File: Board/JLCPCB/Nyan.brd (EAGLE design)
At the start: 86 x 26 mm, 64 parts, among them IC1 74HCT541PW, IC2 STM32F10XCXT6, IC3 74HCT541PW, IC4 ST3485, U2 A4988_STEP, U3 MAX6966, X1 WR-WTB2.0-2_THT-VER, X10 32768, X2 WR-WTB2.0-4_THT_VER, X3 WR-WTB2.0-5_THT-VER, X4 WR-WTB2.0-5_THT-VER, X6 68610614122, X7 68612414422, X8 68610414122, X9 8M

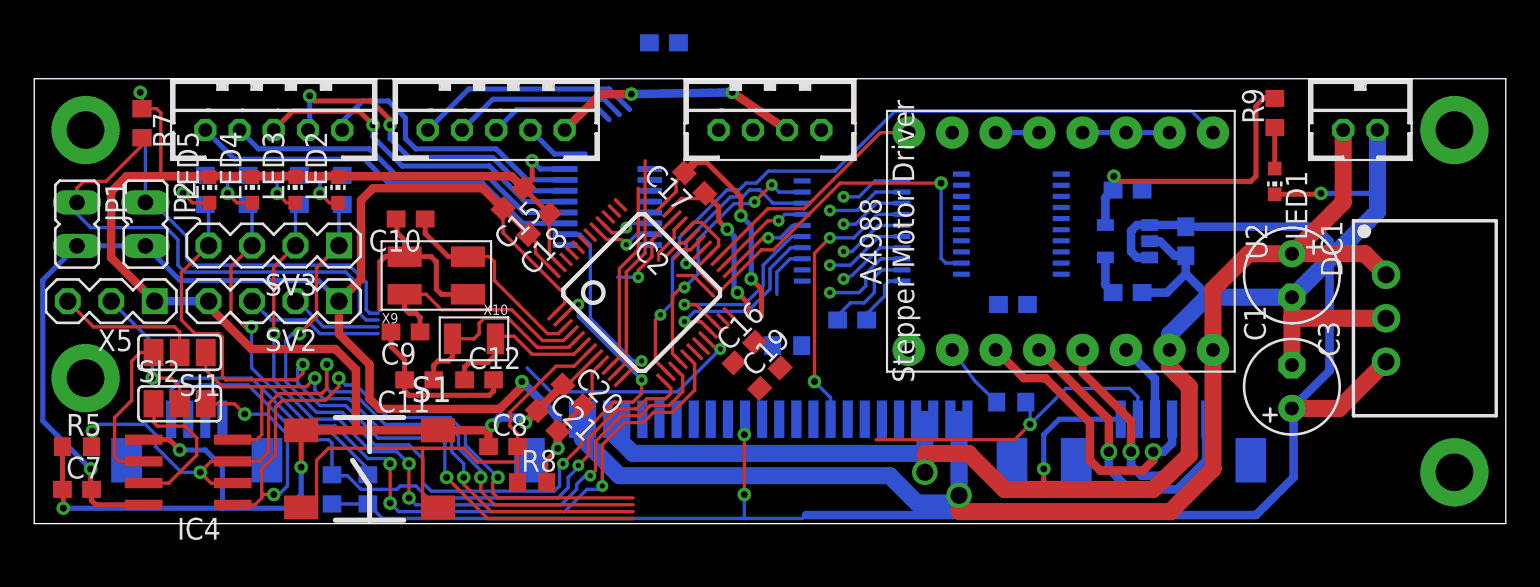
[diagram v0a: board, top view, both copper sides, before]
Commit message: [Board] Layouting of first half (microcontroller side) done.
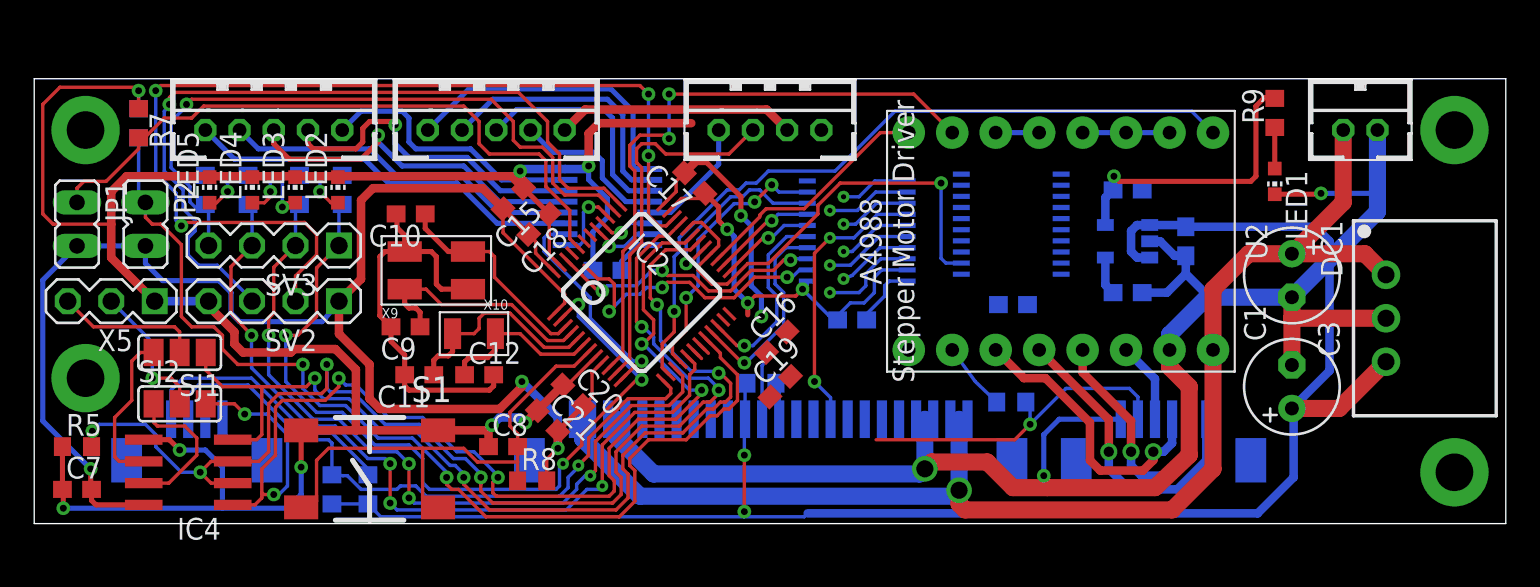
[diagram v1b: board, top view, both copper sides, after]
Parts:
- moved C4 13.7 mm to (33.5, 14.8), turned to 0 degrees
- moved R4 2.66 mm to (42.5, 8.20)
- moved C16 1.99 mm to (43.4, 10.6)
- moved C19 0.78 mm to (43.6, 8.00)
- moved IC1 0.30 mm to (48.1, 17.1)
- moved C10 0.30 mm to (22.0, 18.1)
- moved C9 0.30 mm to (21.7, 11.5)
- moved X9 0.30 mm to (23.5, 14.8)
- moved C11 0.30 mm to (22.5, 8.70)
- moved C12 0.30 mm to (26.0, 8.70)
- moved X10 0.30 mm to (25.7, 11.1)
- moved R6 0.20 mm to (6.10, 23.4)
- moved R7 0.20 mm to (6.10, 23.4)
- moved R8 0.10 mm to (29.1, 2.50)
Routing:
- net SWDIO: track 11.1 -> 59.4 mm, vias 1 -> 4
- net SWCLK: track 8.16 -> 45.9 mm, vias 0 -> 1
- net GND: track 261.5 -> 298.3 mm, vias 12 -> 14
- net MOT_STP: track 11.2 -> 36.5 mm, vias 0 -> 2
- net BOOT1: track 35.9 -> 60.4 mm, vias 1 -> 2
- net TX: track 38.0 -> 59.5 mm, vias 2 -> 4
- net RTS: track 49.9 -> 69.8 mm, vias 4 -> 6
- net RX: track 46.1 -> 65.7 mm, vias 4 -> 6
- net D1: track 0.00 -> 17.3 mm, vias 0 -> 3
- net D2: track 5.70 -> 16.6 mm, vias 0 -> 3
- net BOOT0: track 28.8 -> 38.5 mm
- net BUT_SIG: track 13.2 -> 21.7 mm
- net BUT_LED: track 0.00 -> 7.19 mm
- net LED8: track 7.35 -> 13.4 mm
- net FREE_LED: track 3.78 -> 9.29 mm
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
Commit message: [Board] More layouting
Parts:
- moved R4 5.83 mm to (44.7, 2.80), flipped to the top
- moved C19 2.06 mm to (43.1, 10.0), flipped to the bottom, turned to 90 degrees
- moved C16 0.67 mm to (43.1, 10.0), turned to 90 degrees
- moved R3 0.60 mm to (57.7, 7.10)
- moved C13 0.50 mm to (63.9, 14.0)
- moved C14 0.50 mm to (63.9, 19.0)
- moved C2 0.40 mm to (66.9, 16.5)
- moved R8 0.10 mm to (29.0, 2.50)
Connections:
- net +3V3: now also R1.2, R2.2, R4.2
- net +5V: no longer R1.2, R2.2, R4.2
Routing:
- net +5V: track 119.1 -> 61.1 mm
- net LATCH_5V: track 0.00 -> 30.7 mm, vias 0 -> 2
- net +3V3: track 134.7 -> 155.7 mm, vias 6 -> 9
- net GND: track 298.3 -> 315.2 mm, vias 14 -> 18
- net MOT_THERM: track 20.2 -> 35.8 mm
- net HEAD_THERM: track 2.96 -> 13.2 mm, vias 0 -> 2
- net D5_5V: track 16.4 -> 7.05 mm
- net N$8: track 31.3 -> 27.9 mm
- net DCLK_5V: track 4.96 -> 7.28 mm, vias 1 -> 2
- net D6_5V: track 4.23 -> 6.54 mm, vias 1 -> 2
- net N$19: track 2.24 -> 0.00 mm
- net D1_5V: track 5.75 -> 7.77 mm, vias 1 -> 2
- net D4_5V: track 4.35 -> 6.31 mm, vias 1 -> 2
- net D3_5V: track 5.21 -> 7.18 mm, vias 1 -> 2
- net D2_5V: track 4.43 -> 6.39 mm, vias 1 -> 2
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
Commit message: [Board] almost complete, last gnd and 3v traces missing
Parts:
- moved IC3 0.40 mm to (57.1, 17.1)
- moved C5 0.10 mm to (57.2, 12.7)
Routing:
- net GND: track 315.2 -> 364.9 mm, vias 18 -> 23
- net +5V: track 61.1 -> 109.1 mm, vias 2 -> 5
- net +3V3: track 155.7 -> 187.9 mm, vias 9 -> 10
- net D6_5V: track 6.54 -> 26.5 mm, vias 2 -> 3
- net DCLK_5V: track 7.28 -> 25.7 mm
- net STROBE_5V: track 6.42 -> 23.3 mm
- net D5_5V: track 7.05 -> 18.9 mm
- net D2_5V: track 6.39 -> 17.7 mm
- net D4_5V: track 6.31 -> 17.3 mm
- net D1_5V: track 7.77 -> 16.8 mm
- net D3_5V: track 7.18 -> 16.0 mm
- net MOT_DIR: track 14.3 -> 19.0 mm, vias 0 -> 1
- net N$19: track 0.00 -> 1.74 mm
- net BUT_SIG: track 21.7 -> 23.0 mm, vias 0 -> 1
- net HEAD_THERM: track 13.2 -> 14.3 mm

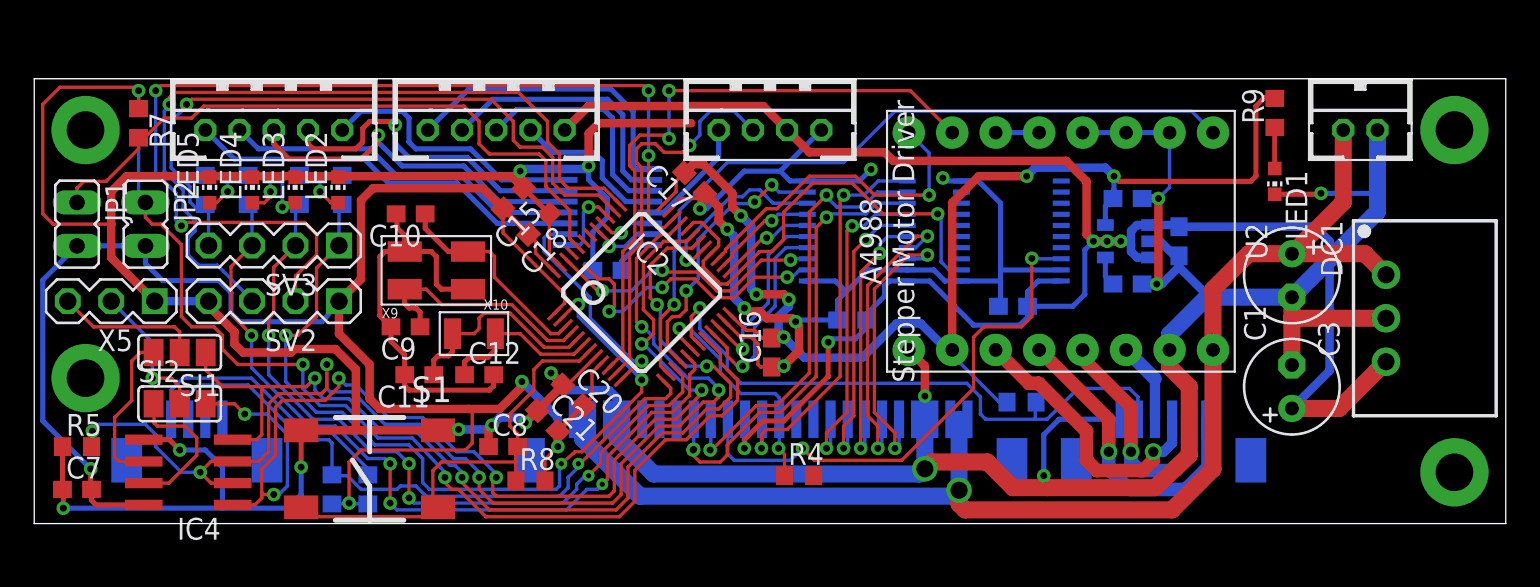
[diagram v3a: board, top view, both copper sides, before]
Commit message: [Board] Layout done
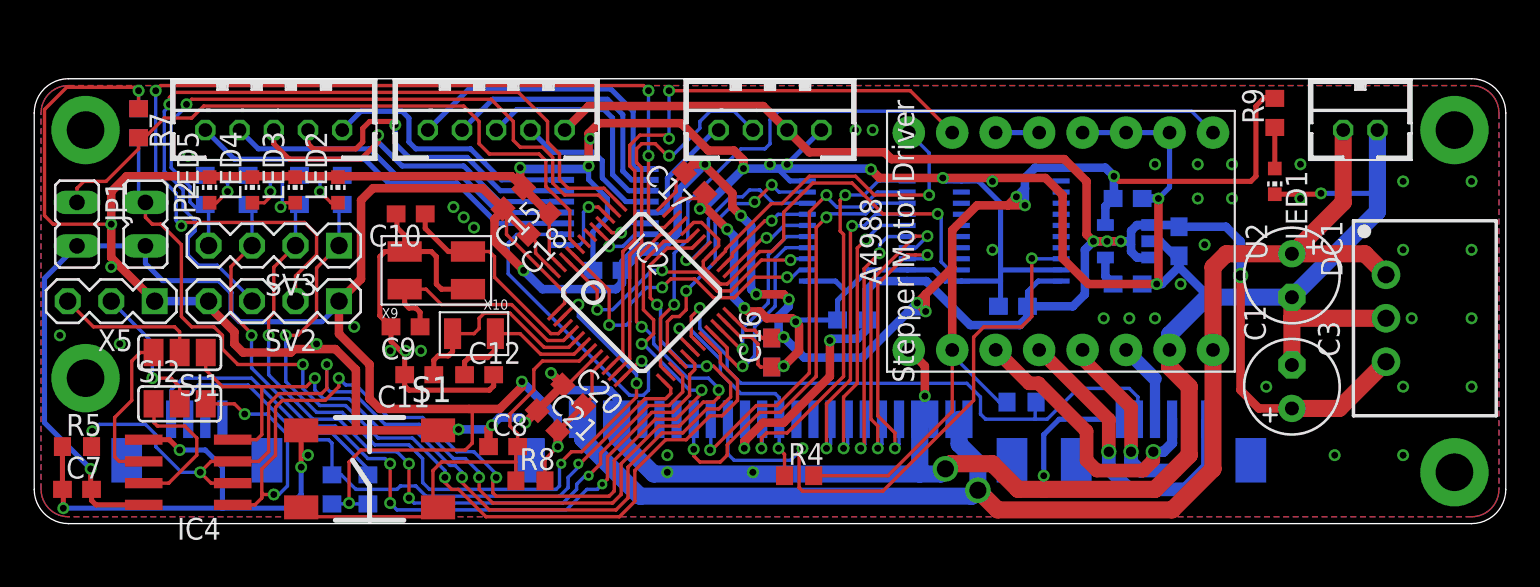
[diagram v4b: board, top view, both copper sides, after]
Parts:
- moved U3 0.20 mm to (33.3, 18.5)
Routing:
- net +3V3: track 187.9 -> 226.2 mm, vias 10 -> 15
- net GND: track 364.9 -> 392.3 mm, vias 23 -> 71
- net LED_CS: track 12.9 -> 20.2 mm
- net LATCH_5V: track 30.9 -> 34.4 mm
- net +5V: track 109.1 -> 106.1 mm, vias 5 -> 6
- net D1: track 17.4 -> 19.5 mm
- net D2: track 16.6 -> 18.2 mm
- net MOT_EN: track 44.3 -> 45.2 mm
- net +12V: track 78.1 -> 78.8 mm
- net D6_5V: vias 3 -> 2
- added copper zone on layer 1, net GND
- added copper zone on layer 16, net GND
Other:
- outline, holes or cut-outs redrawn

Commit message: [Board] Silk Screen Top done
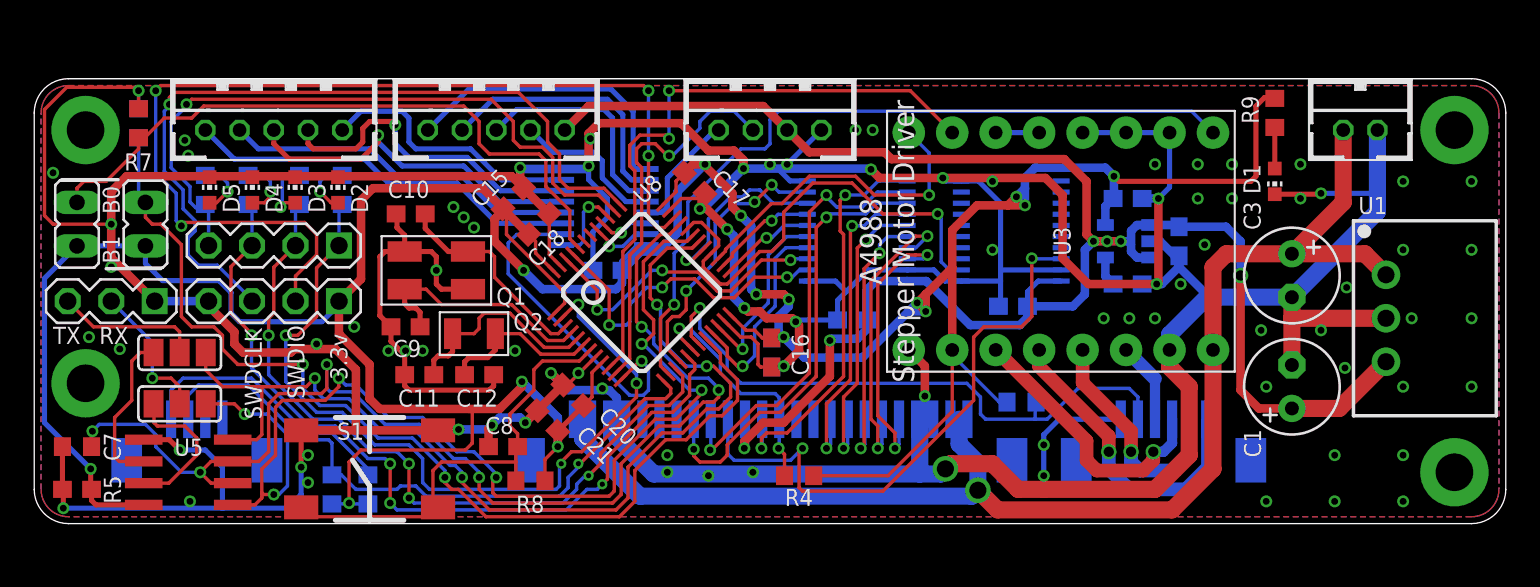
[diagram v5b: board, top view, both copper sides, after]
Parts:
- removed DC1: R-78C5.0-1.0, dc-dc-converter:SIP3
- added U4: MAX6966, meineLibrary:QSOP-16
- U1: value (none) -> R-78C5.0-1.0; device Power:SOT23-5 -> dc-dc-converter:SIP3
- U2: value A4988_STEP -> (none); device robotics:A4988_STEP -> Power:SOT23-5
- U3: value MAX6966 -> A4988_STEP; device meineLibrary:QSOP-16 -> robotics:A4988_STEP
- moved U3 26.8 mm to (60.0, 16.5), flipped to the top, turned to 270 degrees
- moved U1 15.8 mm to (79.0, 12.0), flipped to the top
- moved U2 3.90 mm to (63.9, 16.5), flipped to the bottom
- renumbered IC1 to U6, IC2 to U8, IC3 to U7, IC4 to U5, LED1 to D1, LED2 to D2, LED3 to D3, LED4 to D4, LED5 to D5, X10 to Q2, X9 to Q1
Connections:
- net +12V: now also U1.1, U3.VMOT; no longer DC1.1, U2.VMOT
- net +3V3: now also U2.5, U3.VDD, U4.16; no longer U1.5, U2.VDD, U3.16
- net +5V: now also U2.1, U2.3; no longer DC1.3, U1.1
- net BUT_LED: now also U4.13; no longer U3.13
- net FREE_LED: now also U4.12; no longer U3.12
- net GND: now also U2.2, U3.GND, U3.GND2, U3.MS1, U3.MS2, U3.MS3, U4.8; no longer DC1.2, U2.GND, U2.GND2, U2.MS1, U2.MS2, U2.MS3, U3.8
- net LED1: now also U4.3; no longer U3.3
- net LED2: now also U4.4; no longer U3.4
- net LED3: now also U4.5; no longer U3.5
- net LED4: now also U4.6; no longer U3.6
- net LED5: now also U4.7; no longer U3.7
- net LED6: now also U4.9; no longer U3.9
- net LED7: now also U4.10; no longer U3.10
- net LED8: now also U4.11; no longer U3.11
- net LED_CLK: now also U4.1; no longer U3.1
- net LED_CS: now also U4.2; no longer U3.2
- net LED_MISO: now also U4.14; no longer U3.14
- net LED_MOSI: now also U4.15; no longer U3.15
- net M1A: now also U3.1A; no longer U2.1A
- net M1B: now also U3.1B; no longer U2.1B
- net M2A: now also U3.2A; no longer U2.2A
- net M2B: now also U3.2B; no longer U2.2B
- net MOT_DIR: now also U3.DIR; no longer U2.DIR
- net MOT_EN: now also U3./EN; no longer U2./EN
- net MOT_STP: now also U3.STEP; no longer U2.STEP
- net N$19: now also U2.4; no longer U1.4
- net N$2: now also U3./RST, U3./SLP; no longer U2./RST, U2./SLP
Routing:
- net GND: vias 71 -> 88
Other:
- board text added: "3.3v"
- board text added: "B0"
- board text added: "B1"
- board text added: "RX"
- board text added: "SWDCLK"
- board text added: "SWDIO"
- board text added: "TX"
